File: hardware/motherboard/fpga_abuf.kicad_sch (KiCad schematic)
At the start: 8 parts, among them U15 SN74ALVC164245, U16 SN74ALVC164245, U17 SN74ALVC164245, U18 SN74ALVC164245

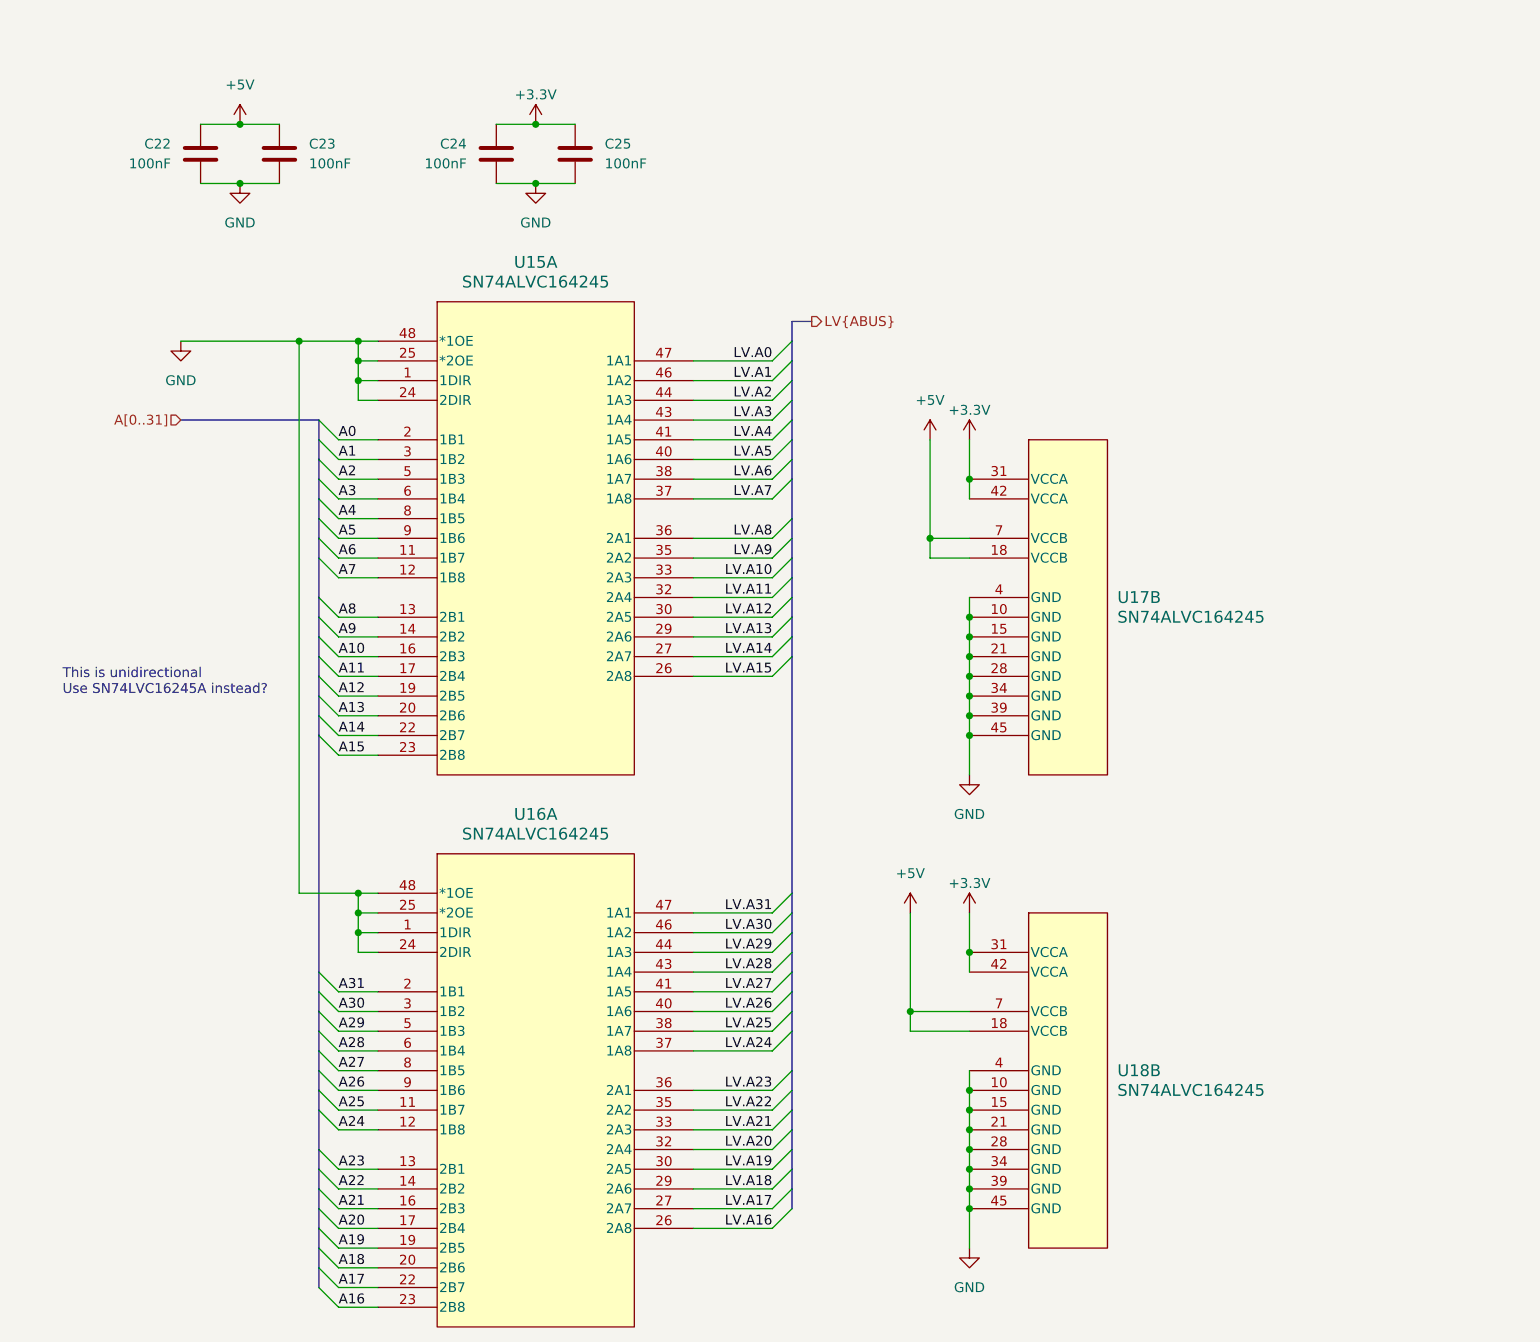
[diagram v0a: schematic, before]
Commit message: restructure, create minimum board project
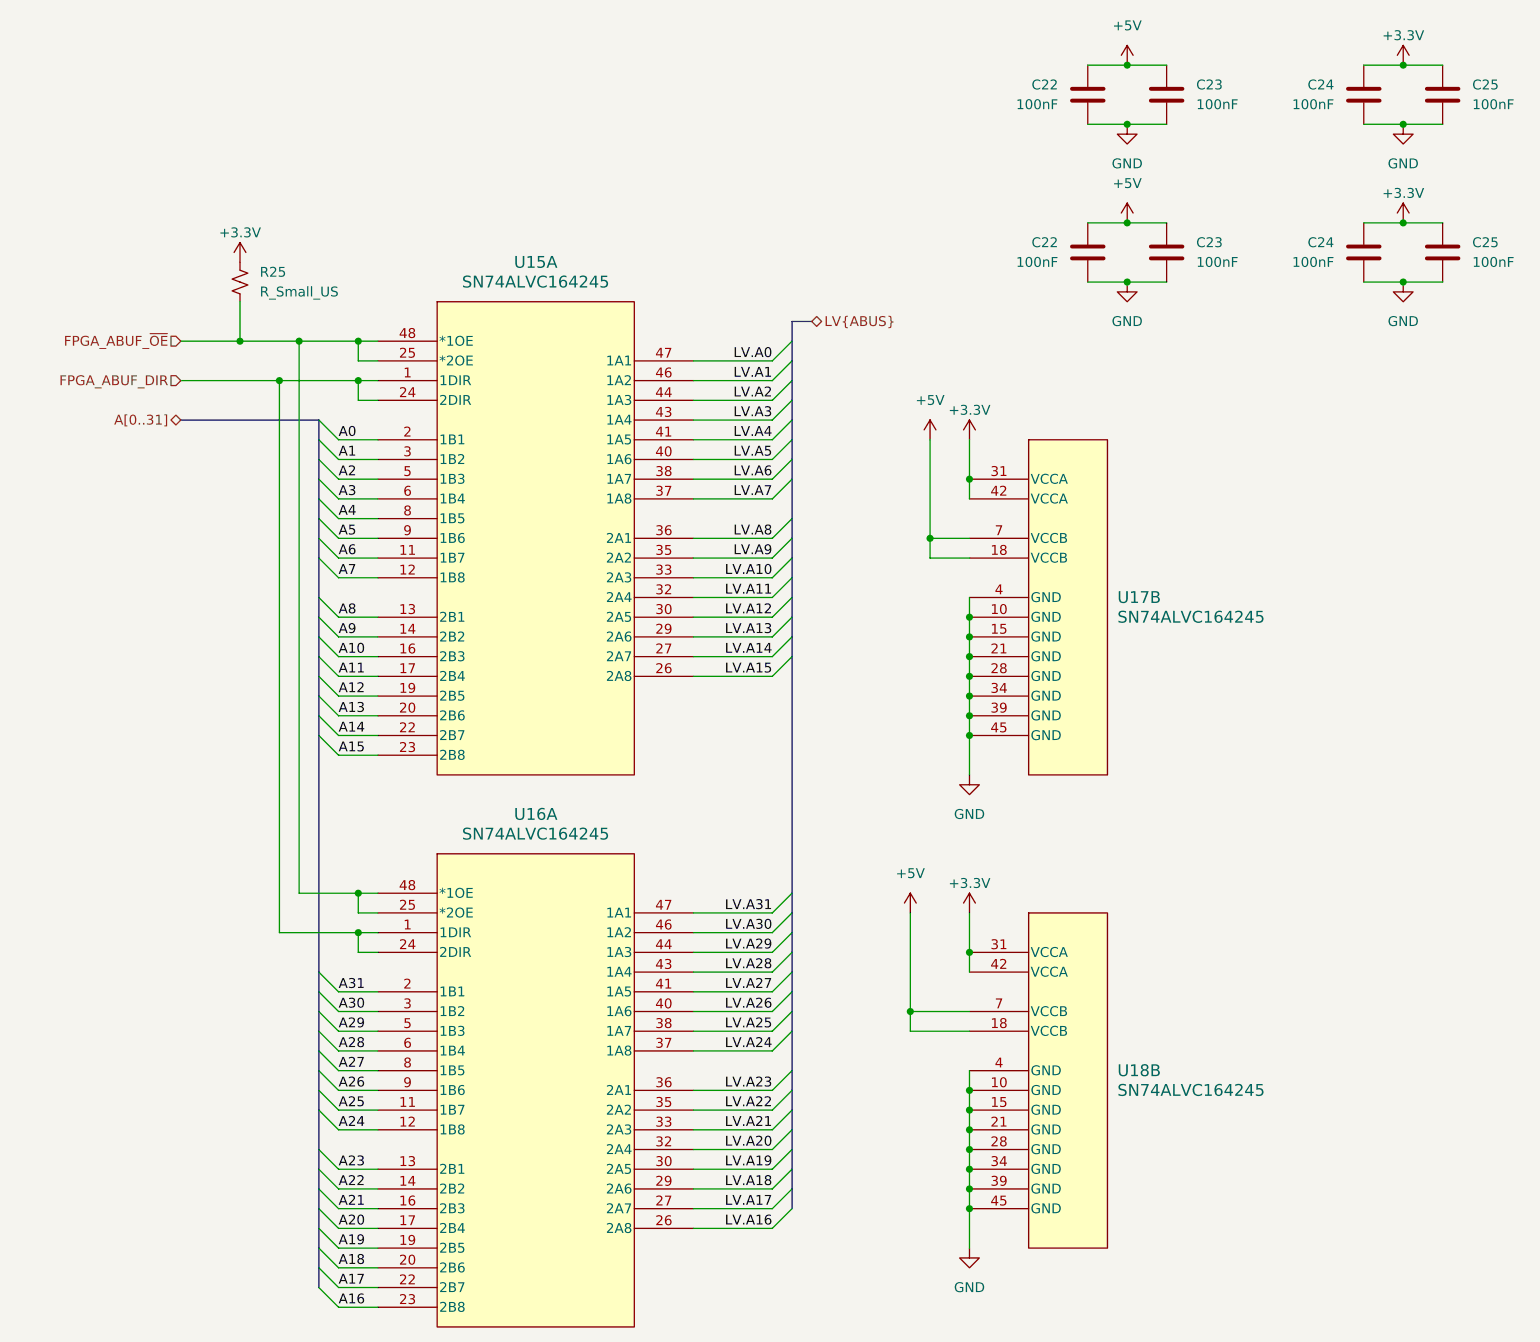
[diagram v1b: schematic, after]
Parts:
- added C22, C23, C24, C25: 100nF, symbol Device:C
- added R25: R_Small_US, symbol Device:R_Small_US
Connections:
- net +3.3V: now also C24.1, C25.1, R25.1
- net +5V: now also C22.1, C23.1
- net GND: now also C22.2, C23.2, C24.2, C25.2; no longer U15.1 (1DIR), U15.24 (2DIR), U15.25 (*2OE), U15.48 (*1OE), U16.1 (1DIR), U16.24 (2DIR), U16.25 (*2OE), U16.48 (*1OE)
- new net FPGA_ABUF_DIR: U15.1 (1DIR), U15.24 (2DIR), U16.1 (1DIR), U16.24 (2DIR)
- new net FPGA_ABUF_~{OE}: R25.2, U15.25 (*2OE), U15.48 (*1OE), U16.25 (*2OE), U16.48 (*1OE)
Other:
- note removed: "This is unidirectional Use SN74LVC16245A instead?"
- moved on the sheet: C22, C23, C24, C25

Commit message: work on testboard, move 3d models
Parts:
- renumbered C22 to C24, C23 to C25, C24 to C26, C25 to C27, C22 to C61, C23 to C62, C24 to C63, C25 to C64, U17 to U16, U15 to U16, U16 to U18
